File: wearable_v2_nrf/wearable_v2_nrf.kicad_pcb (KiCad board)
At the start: 4 copper layers, 40.2 x 40 mm, 52 parts, among them IC1 MCP73831T-2ACI_OT, J1 Conn_01x04, J2 217175-0001, J3 Conn_01x03, M1 Motor_DC, Q1 PMOS, Q2 NPN, SW1 Reset, U1 nRF52811-QCxx, U3 BMI270, U4 MCP1700x-330xxMB, U5 2450AT18A100E, Y1 ABM10W-32.0000MHZ-8-B1U-T3, Y2 Crystal

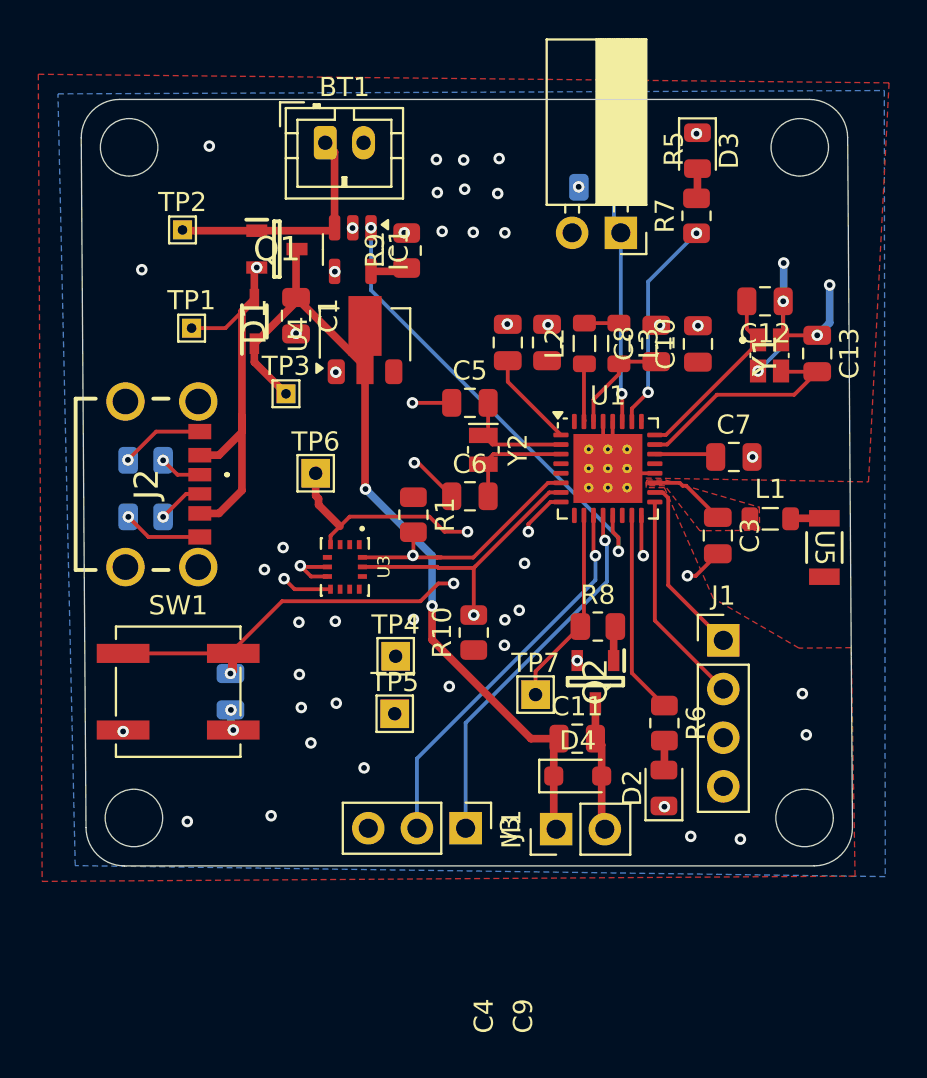
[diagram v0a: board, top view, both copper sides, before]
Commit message: changes
fixed mosfet symbol-footprint,
connection jst->molex pico,
made HSC closer
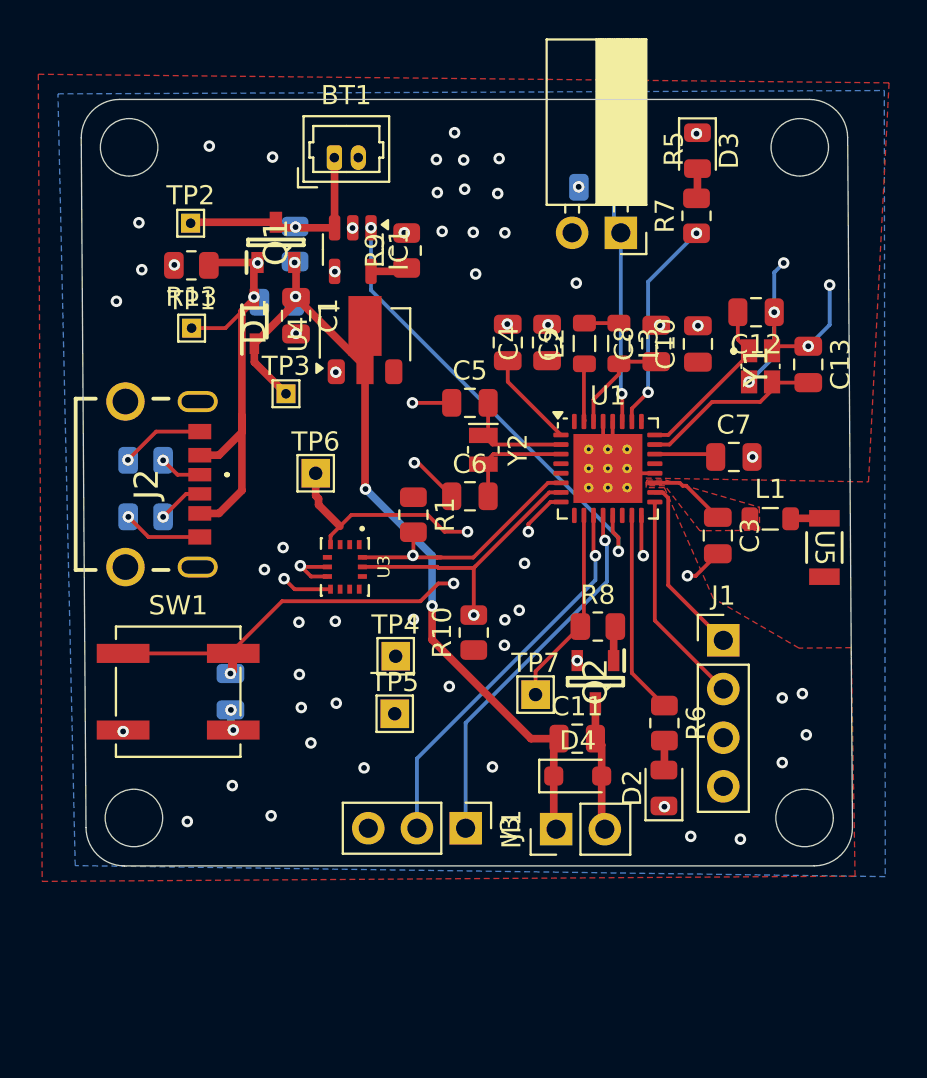
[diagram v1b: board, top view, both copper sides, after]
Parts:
- added R11: 0, Resistor_SMD:R_0805_2012Metric, B.Cu at (92.2, 58.9)
- added R12: 0, Resistor_SMD:R_0805_2012Metric, B.Cu at (93.2, 55.9)
- added R13: 10k, Resistor_SMD:R_0805_2012Metric, F.Cu at (87.8, 57.0)
- BT1: footprint Connector_JST:JST_PH_B2B-PH-K_1x02_P2.00mm_Vertical -> Connector_Molex:Molex_PicoBlade_53047-0210_1x02_P1.25mm_Vertical
- C12, C13, C5, C6: value 10p -> 12p
- moved BT1 0.91 mm to (95.2, 51.4)
- moved C13 0.74 mm to (120.0, 62.1)
- moved Y1 0.74 mm to (117.3, 62.2)
- moved C12 0.74 mm to (117.3, 59.4)
- moved TP2 0.55 mm to (87.8, 54.8)
- moved Q1 0.35 mm to (92.2, 55.8), turned to 90 degrees
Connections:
- Q1 pad 1: /VBAT+ -> /VBUS
- Q1 pad 2: /VBUS -> VCC
- Q1 pad 3: VCC -> /VBAT+
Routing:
- net /VBUS: track 26.3 -> 29.7 mm, vias 2 -> 3
- net /X2: track 12.0 -> 9.62 mm
- net GND: track 37.3 -> 38.9 mm, vias 31 -> 42
- net /VBAT+: track 12.7 -> 11.4 mm, vias 0 -> 1
- net VCC: track 43.6 -> 43.0 mm, vias 2 -> 4
- net /X1: track 9.79 -> 9.25 mm
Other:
- board text added: "Wearable V2 Designed by Raymond Jiang, Yilin Jin, Anna Guo, Varun Srinivasan, Richard Nguyen"

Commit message: v2 revisions for nrf pcb
fix imu, fix adc
includes new firmware for nrf52811
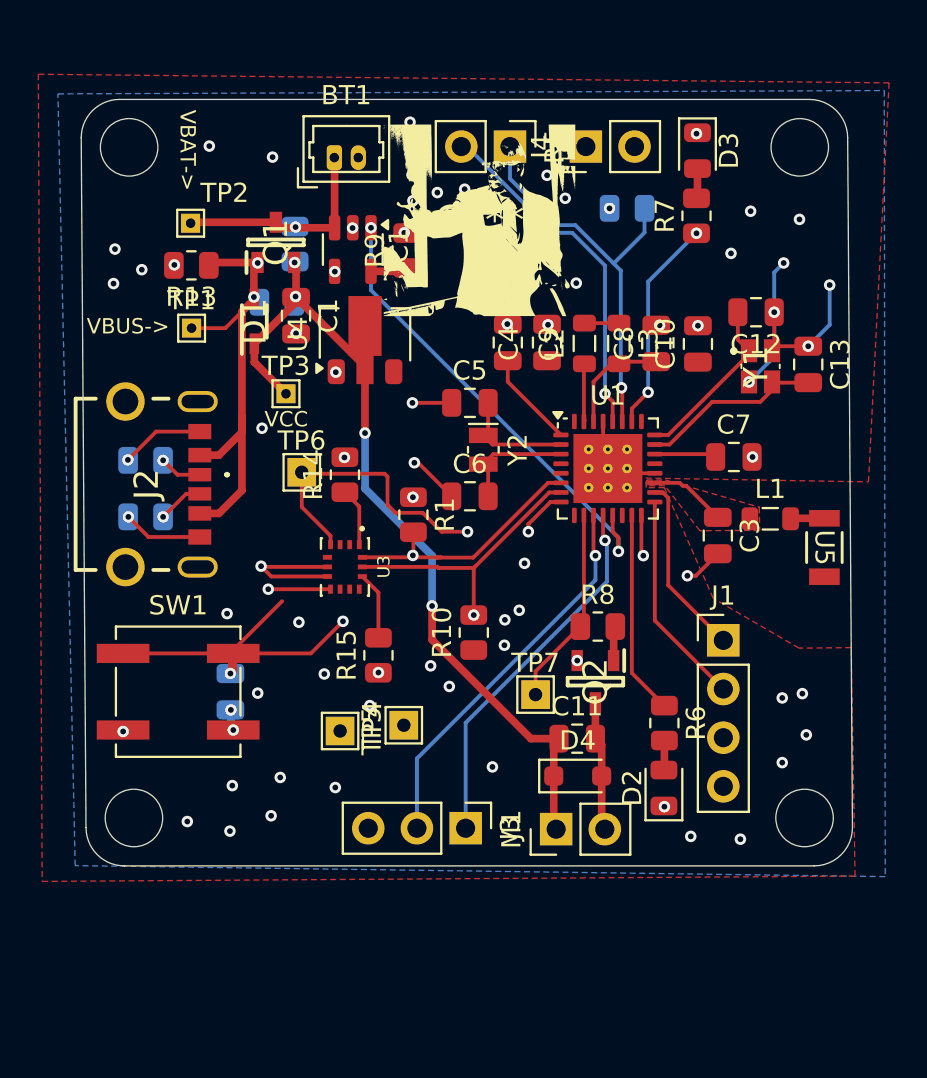
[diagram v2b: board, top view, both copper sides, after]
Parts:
- added G***: LOGO, A_wearables:valvano_final, F.Cu at (102.8, 54.6)
- added J4: Conn_01x02, Connector_PinHeader_2.54mm:PinHeader_1x02_P2.54mm_Vertical, F.Cu at (108.4, 50.8)
- added R14: 10k, Resistor_SMD:R_0805_2012Metric, F.Cu at (95.8, 67.9)
- added R15: 10k, Resistor_SMD:R_0805_2012Metric, F.Cu at (97.5, 77.3)
- R5: footprint Connector_PinSocket_2.54mm:PinSocket_1x02_P2.54mm_Horizontal -> Connector_PinHeader_2.54mm:PinHeader_1x02_P2.54mm_Vertical
- moved R5 7.33 mm to (104.4, 50.8)
- moved TP4 3.62 mm to (98.9, 81.0), turned to 90 degrees
- moved TP5 2.99 mm to (95.5, 81.3), turned to -90 degrees
- moved R4 1.94 mm to (110.5, 54.0)
- moved TP6 0.73 mm to (93.5, 67.8)
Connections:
- R5 pad 2: GND -> /ADC1_N
- U1 pad 28: GND -> /ADC1_N
- U3 pad 1: unconnected-(U3-SDO-Pad1) -> Net-(U3-SDO)
- U3 pad 12: unconnected-(U3-CSB-Pad12) -> Net-(U3-CSB)
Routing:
- net /ADC1_N: track 0.00 -> 18.4 mm, vias 0 -> 1
- net /I2C1_SCL: track 21.3 -> 30.2 mm
- net /ADC1_P: track 12.4 -> 20.9 mm
- net /NRST: track 33.8 -> 37.4 mm
- net Net-(U3-CSB): track 0.00 -> 3.55 mm
- net /I2C1_SDA: track 19.2 -> 22.7 mm
- net /INT1: track 17.5 -> 20.9 mm
- net Net-(U3-SDO): track 0.00 -> 3.05 mm
- net GND: track 38.9 -> 41.7 mm, vias 42 -> 45
- net +3.3V: track 2.80 -> 3.40 mm, vias 29 -> 33
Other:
- board text added: "VBAT->"
- board text added: "VBUS->"
- board text added: "VCC"

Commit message: final nrf board edits + ble sniffer py script
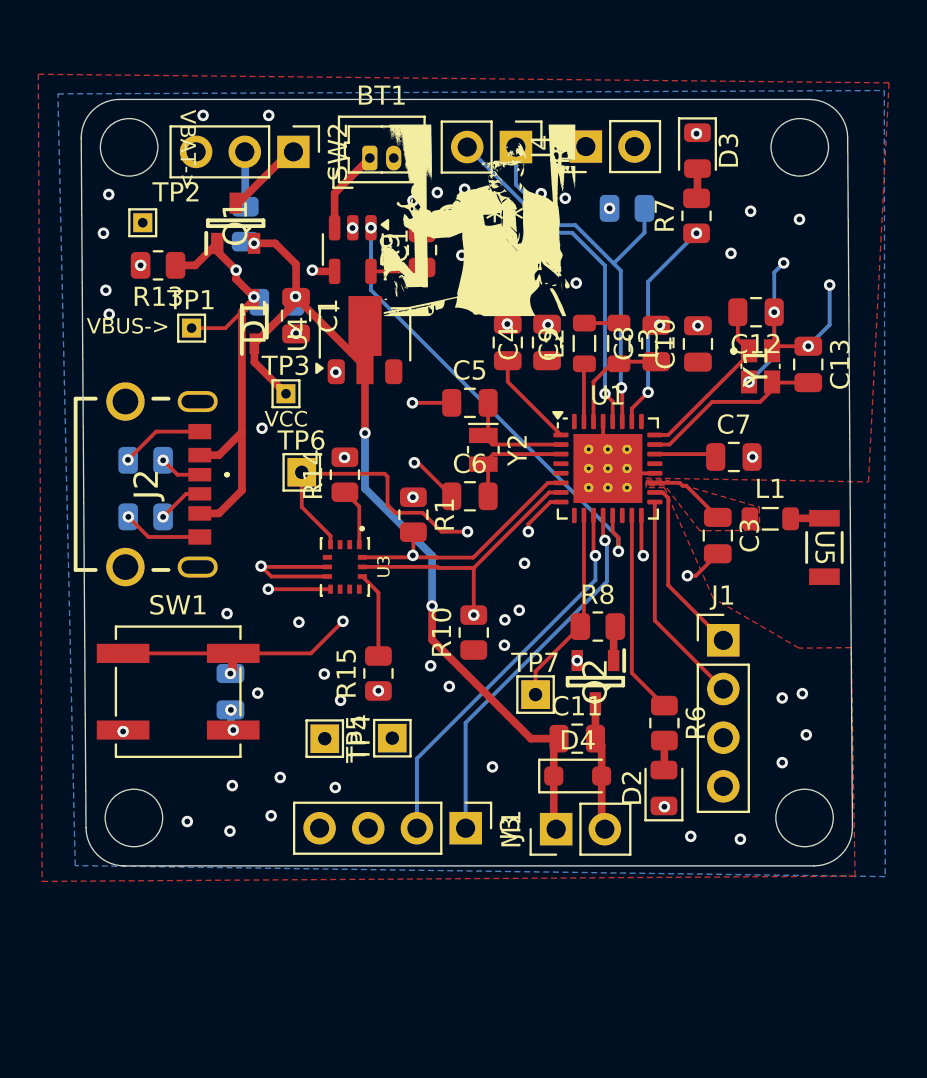
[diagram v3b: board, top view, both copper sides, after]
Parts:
- added SW2: SW_SPDT, Connector_PinHeader_2.54mm:PinHeader_1x03_P2.54mm_Vertical, F.Cu at (93.1, 51.0)
- J3: value Conn_01x03 -> Conn_01x04; footprint Connector_PinHeader_2.54mm:PinHeader_1x03_P2.54mm_Vertical -> Connector_PinHeader_2.54mm:PinHeader_1x04_P2.54mm_Vertical
- moved R12 2.80 mm to (90.6, 54.8)
- moved TP2 2.50 mm to (85.2, 54.8)
- moved Q1 2.33 mm to (90.1, 54.8)
- moved BT1 1.85 mm to (97.1, 51.4)
- moved R13 1.74 mm to (86.0, 57.0)
- moved R15 0.95 mm to (97.5, 78.3)
- moved TP4 0.90 mm to (98.3, 81.7)
- moved TP5 0.89 mm to (94.8, 81.7)
- moved R9 0.80 mm to (99.8, 56.2)
- moved R5 0.31 mm to (104.7, 50.8)
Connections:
- J3 pad 3: GND -> +3.3V
- Q1 pad 3: /VBAT+ -> Net-(Q1-D)
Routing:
- net /VBAT+: track 11.4 -> 21.6 mm, vias 1 -> 0
- net Net-(Q1-D): track 0.00 -> 3.86 mm
- net /NRST: track 37.4 -> 33.6 mm
- net VCC: track 43.0 -> 45.5 mm
- net /VBUS: track 29.7 -> 31.1 mm
- net Net-(U3-CSB): track 3.55 -> 4.50 mm
- net /prog: track 1.86 -> 2.75 mm
- net /I2C1_SDA: track 22.7 -> 23.3 mm

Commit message: final pcb design :)
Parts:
- added R16: 0, Resistor_SMD:R_0805_2012Metric, F.Cu at (103.9, 55.8)
- moved IC1 0.60 mm to (96.2, 55.5)
- moved R9 0.45 mm to (99.8, 56.6)
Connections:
- IC1 pad 1: /STAT -> Net-(IC1-STAT)
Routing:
- net Net-(IC1-STAT): track 0.00 -> 7.01 mm
- net /STAT: track 24.2 -> 21.5 mm
- net /VBAT+: track 21.6 -> 21.0 mm
